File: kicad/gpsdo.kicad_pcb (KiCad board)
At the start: 2 copper layers, 76.2 x 30.5 mm, 54 parts, among them J1 Conn_Coaxial, J2 Conn_01x04_Male, J3 Conn_01x04_Male, J4 Conn_01x04_Male, J5 Conn_01x04_Male, J6 Conn_01x04_Male, U1 MSP430F5171IDA, U10 74AUC1G79, U11 47L64, U12 47L64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

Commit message: update pcb layout
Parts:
- removed C8: 100n, Resistor_SMD:R_0603_1608Metric
- removed R4, R5, R6, R7: 1.5k, Resistor_SMD:R_0603_1608Metric
- removed U5: LTC4317, Package_DFN_QFN:DFN-16-1EP_3x5mm_P0.5mm_EP1.66x4.4mm
- moved C21 0.78 mm to (77.5, 52.3), turned to 0 degrees
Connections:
- U1 pad 23: /EN2 -> Net-(U1-Pad23)
- U1 pad 24: /EN1 -> Net-(U1-Pad24)
- U11 pad 5: /SDA1 -> /SDA
- U11 pad 6: /SCL1 -> /SCL
- U11 pad 7: GND -> Net-(U11-Pad7)
- U12 pad 5: /SDA1 -> /SDA
- U12 pad 6: /SCL1 -> /SCL
- U2 pad 16: /SDA2 -> /SDA
- U2 pad 17: /SCL2 -> /SCL
- U3 pad 7: /SDA1 -> /SDA
- U3 pad 8: /SCL1 -> /SCL
- U4 pad 1: /SDA1 -> /SDA
- U4 pad 6: /SCL1 -> /SCL
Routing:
- net /SCL1: track 74.3 -> 0.00 mm, vias 4 -> 0
- net /SCL: track 15.3 -> 88.9 mm, vias 0 -> 4
- net /SDA1: track 73.0 -> 0.00 mm, vias 4 -> 0
- net /SDA: track 18.5 -> 90.2 mm, vias 2 -> 4
- net /SCL2: track 27.2 -> 0.00 mm, vias 4 -> 0
- net /EN2: track 25.5 -> 0.00 mm, vias 2 -> 0
- net /SDA2: track 25.4 -> 0.00 mm, vias 2 -> 0
- net /EN1: track 22.3 -> 0.00 mm, vias 2 -> 0
- net GND: track 70.1 -> 64.1 mm, vias 52 -> 48
- net +3V3: track 27.4 -> 25.3 mm, vias 2 -> 0
- net Net-(U11-Pad7): track 0.00 -> 1.64 mm, vias 0 -> 1
- net /uTXD: track 40.2 -> 39.4 mm
- net /uRXD: track 42.5 -> 41.9 mm
- net gPPS: track 21.3 -> 20.7 mm
- net Net-(C21-Pad2): track 2.59 -> 2.01 mm

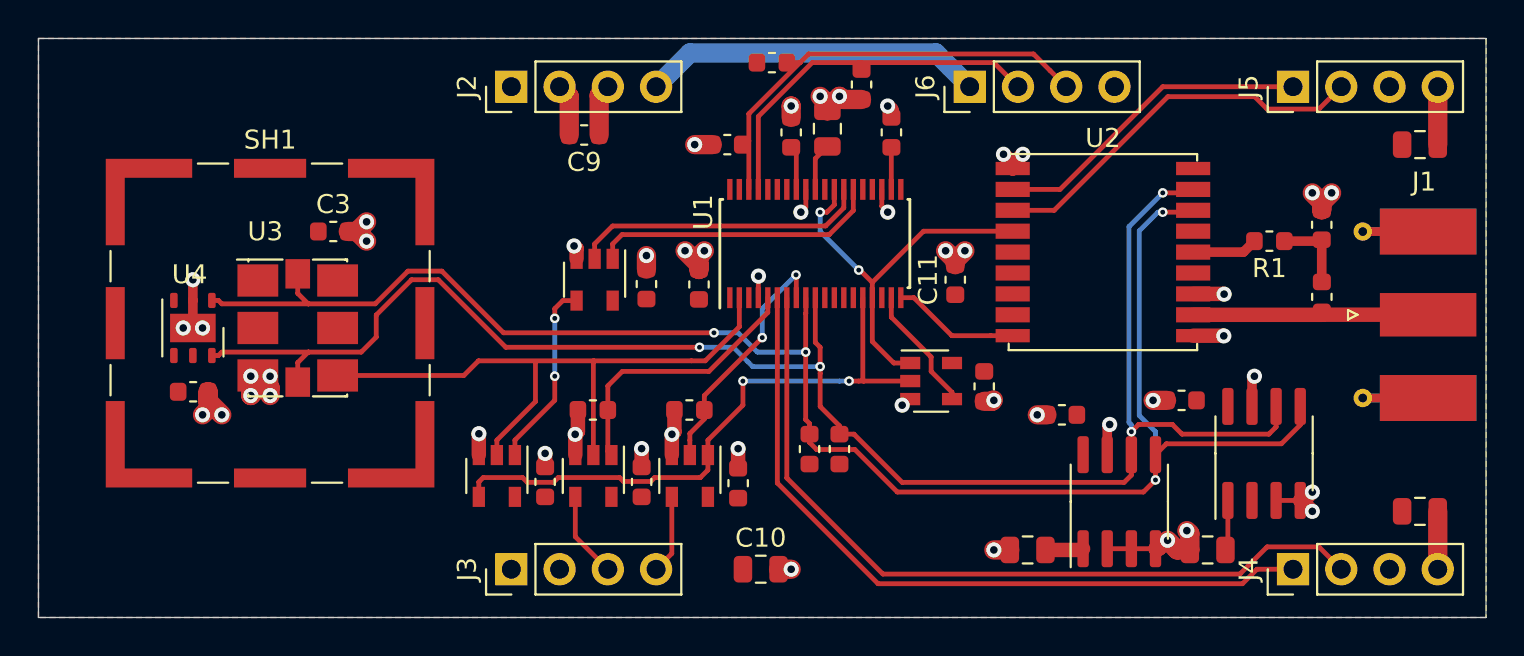
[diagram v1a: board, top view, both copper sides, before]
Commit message: remove extra EERAM
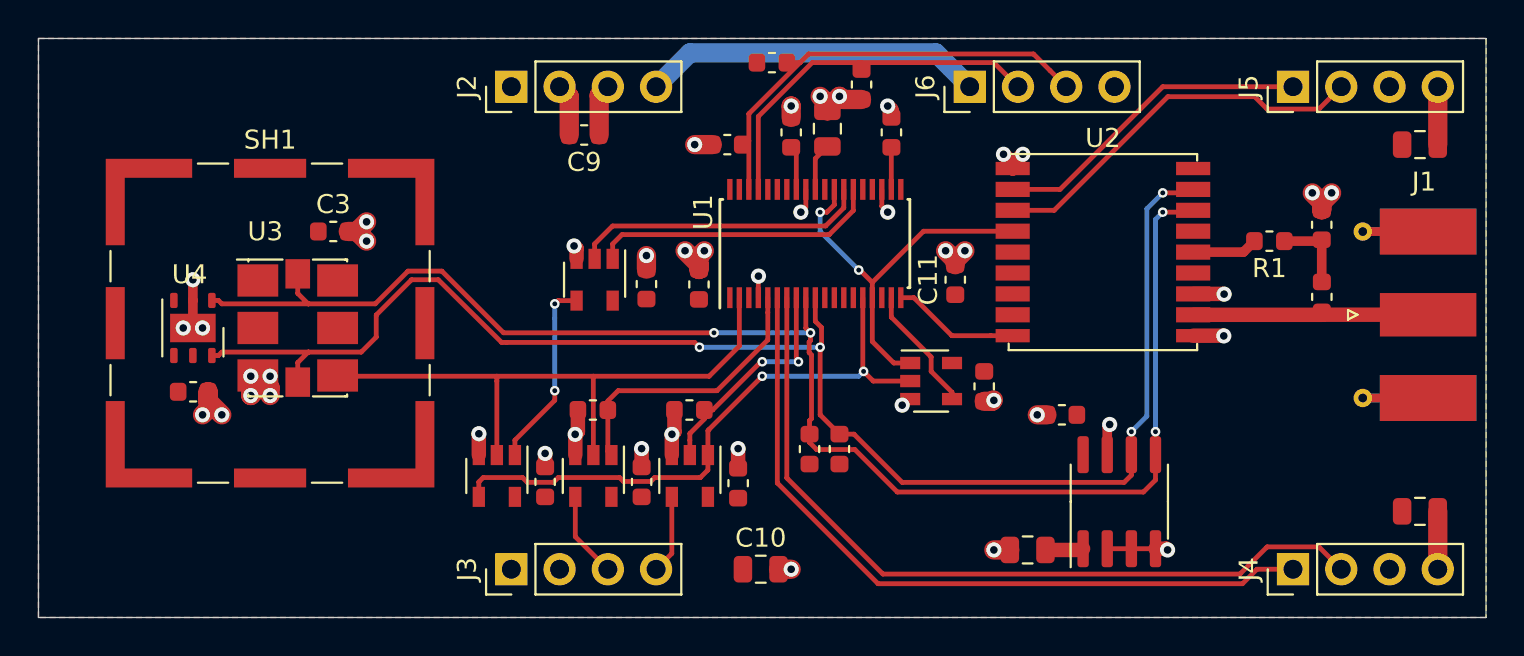
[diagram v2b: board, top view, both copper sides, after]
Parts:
- removed C16: 100n, Resistor_SMD:R_0603_1608Metric
- removed C22: 22u, Capacitor_SMD:C_0805_2012Metric
- removed U12: 47L64, Package_SO:SOIC-8_3.9x4.9mm_P1.27mm
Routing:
- net /SDA: track 90.2 -> 78.8 mm
- net /SCL: track 88.9 -> 79.2 mm
- net GND: track 64.1 -> 56.1 mm, vias 48 -> 43
- net Net-(C22-Pad2): track 2.66 -> 0.00 mm
- net CLK_25M: track 34.5 -> 32.7 mm
- net EN_PPS: track 13.0 -> 12.2 mm

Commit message: update pcb layout
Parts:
- C10, C19, C20: value 10u -> 22u
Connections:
- net Net-(J1-Pad1) renamed /gANT
- net Net-(U1-Pad19) renamed /gRST
- net Net-(U8-Pad1) renamed /uPPS
- U1 pad 11: Net-(U1-Pad11) -> +3V3
- U1 pad 12: Net-(U1-Pad12) -> +3V3
- U1 pad 13: Net-(U1-Pad13) -> +3V3
- U1 pad 14: Net-(U1-Pad14) -> +3V3
- U1 pad 2: CLK_25M -> Net-(U1-Pad2)
- U1 pad 20: Net-(U1-Pad20) -> +3V3
- U1 pad 23: Net-(U1-Pad23) -> +3V3
- U1 pad 24: Net-(U1-Pad24) -> +3V3
- U1 pad 3: Net-(U1-Pad3) -> CLK_25M
- U1 pad 32: Net-(U1-Pad32) -> +3V3
- U1 pad 33: Net-(U1-Pad33) -> +3V3
- U1 pad 34: Net-(U1-Pad34) -> +3V3
- U1 pad 37: Net-(U1-Pad37) -> +3V3
- U1 pad 38: Net-(U1-Pad38) -> +3V3
- U11 pad 7: Net-(U11-Pad7) -> GND
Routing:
- net Net-(U11-Pad7): track 1.64 -> 0.00 mm, vias 1 -> 0
- net GND: track 56.1 -> 57.5 mm, vias 43 -> 44
- net gPPS: track 20.7 -> 20.6 mm, vias 2 -> 3

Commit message: update pcb layout
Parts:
- removed C12, C13, C14, C15, C17, C9: 100n, Resistor_SMD:R_0603_1608Metric
- removed R8, R9: 15k, Resistor_SMD:R_0603_1608Metric
- removed U10, U8: 74AUC1G79, Package_TO_SOT_SMD:SOT-23-5
- removed U6, U7: 74LVC1G08, Package_TO_SOT_SMD:SOT-23-5
- removed U9: 74LVC1G86, Package_TO_SOT_SMD:SOT-23-5
- moved C10 24.3 mm to (53.9, 31.0), turned to 180 degrees
- moved C21 13.1 mm to (66.3, 45.5), turned to 90 degrees
- moved R3 12.5 mm to (78.2, 49.3)
- moved U11 11.4 mm to (71.4, 46.5), turned to 0 degrees
- moved R2 10.7 mm to (78.2, 46.3), turned to 270 degrees
- moved C18 3.07 mm to (76.2, 45.2), turned to 270 degrees
- moved C6 1.11 mm to (59.4, 39.1), turned to 180 degrees
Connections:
- J3 pad 3: /CLK -> CLK
- J3 pad 4: /PPS -> PPS
- U1 pad 15: oPPS -> PPS
- U1 pad 17: Net-(U1-Pad17) -> +3V3
- U1 pad 18: dPPS -> +3V3
- U1 pad 25: iPPS -> +3V3
- U1 pad 26: mPPS -> gPPS
- U1 pad 27: gPPS -> PPS
- U1 pad 3: CLK_25M -> CLK
- U1 pad 5: EN_CLK -> +3V3
- U1 pad 8: EN_PPS -> +3V3
- U3 pad 4: CLK_25M -> CLK
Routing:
- net CLK: track 0.00 -> 34.8 mm
- net CLK_25M: track 32.9 -> 0.00 mm
- net oPPS: track 31.6 -> 0.00 mm, vias 2 -> 0
- net PPS: track 0.00 -> 27.2 mm, vias 0 -> 2
- net mPPS: track 15.7 -> 0.00 mm
- net iPPS: track 15.3 -> 0.00 mm
- net EN_CLK: track 15.1 -> 0.00 mm
- net EN_PPS: track 12.2 -> 0.00 mm, vias 2 -> 0
- net GND: track 57.5 -> 46.8 mm, vias 44 -> 32
- net /uPPS: track 10.0 -> 0.00 mm, vias 2 -> 0
- net dPPS: track 6.66 -> 0.00 mm
- net gPPS: track 20.6 -> 14.5 mm, vias 3 -> 0
- net /SDA: track 79.0 -> 73.8 mm, vias 4 -> 2
- net /SCL: track 79.3 -> 74.7 mm, vias 4 -> 2
- net /CLK: track 4.52 -> 0.00 mm
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
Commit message: update pcb layout
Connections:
- U1 pad 15: PPS -> gPPS
- U1 pad 16: gPPS -> PPS
- U1 pad 17: +3V3 -> /gRST
- U1 pad 18: +3V3 -> PPS
- U1 pad 19: /gRST -> gPPS
- U1 pad 26: gPPS -> +3V3
- U1 pad 27: PPS -> +3V3
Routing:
- net PPS: track 27.2 -> 23.8 mm
- net gPPS: track 14.5 -> 11.5 mm
- net /gRST: track 7.19 -> 8.19 mm

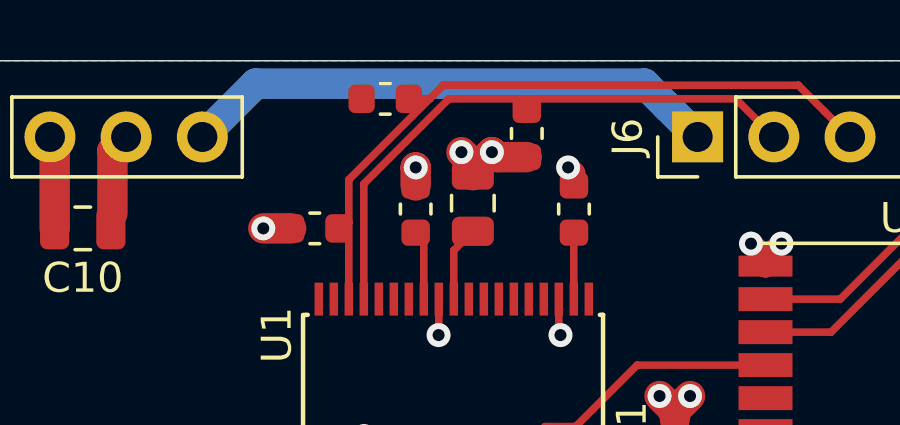
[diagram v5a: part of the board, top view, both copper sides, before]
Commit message: cleanup board layout
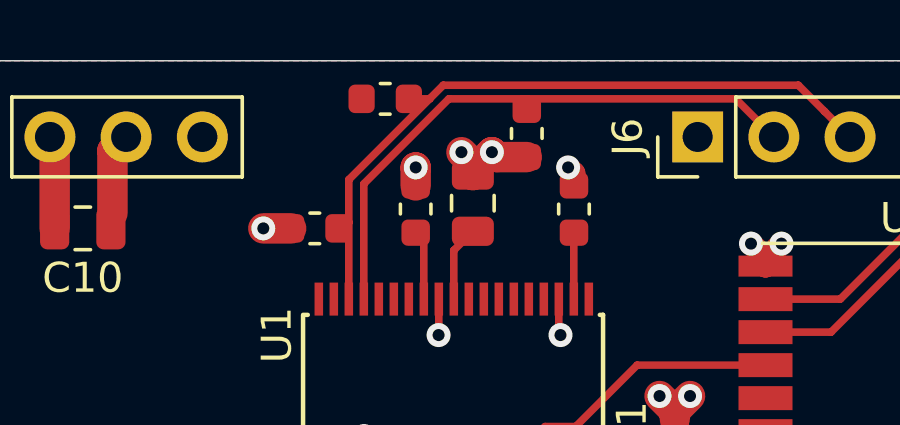
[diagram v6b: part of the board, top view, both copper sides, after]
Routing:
- net +3V3: track 27.1 -> 9.13 mm
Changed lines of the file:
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@@
     (thickness 1.6)
     (drawings 4)
-    (tracks 265)
+    (tracks 261)
     (zones 0)
     (modules 32)
@@
   (segment (start 54.915 28.397) (end 55.372 27.94) (width 1.016) (layer F.Cu) (net 2))
   (segment (start 54.915 30.48) (end 54.915 28.397) (width 1.016) (layer F.Cu) (net 2))
-  (segment (start 73.406 26.924) (end 74.422 27.94) (width 1.016) (layer B.Cu) (net 2))
-  (segment (start 72.644 26.162) (end 73.406 26.924) (width 1.016) (layer B.Cu) (net 2))
-  (segment (start 59.69 26.162) (end 72.644 26.162) (width 1.016) (layer B.Cu) (net 2))
-  (segment (start 57.912 27.94) (end 59.69 26.162) (width 1.016) (layer B.Cu) (net 2))
   (segment (start 65.294 39.045) (end 65.294 39.1) (width 0.254) (layer F.Cu) (net 2))
   (segment (start 63.794 39.045) (end 63.794 39.838) (width 0.254) (layer F.Cu) (net 2))

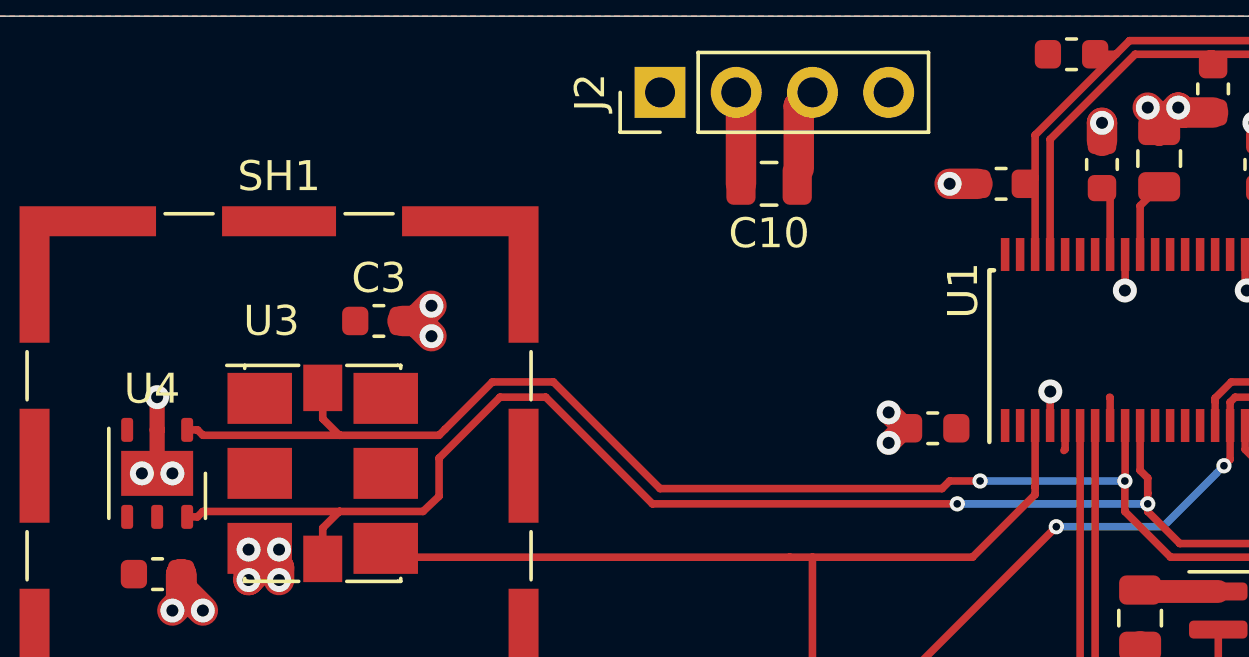
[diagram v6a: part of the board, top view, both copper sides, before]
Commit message: change Si549 to Si544
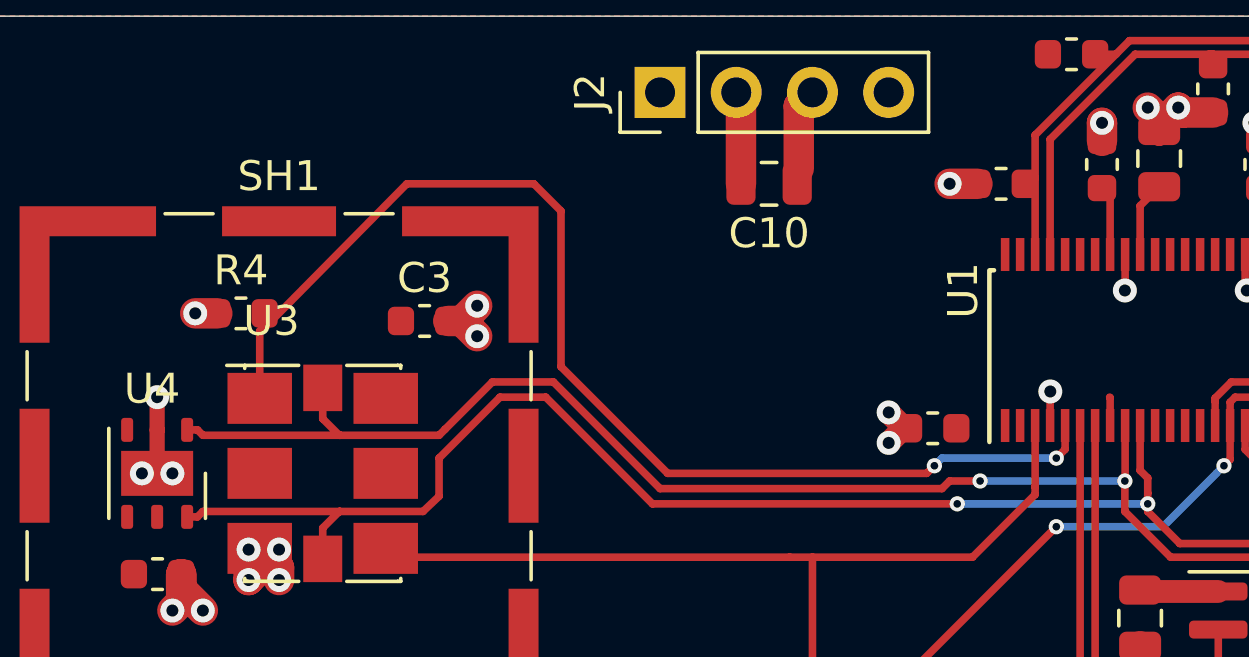
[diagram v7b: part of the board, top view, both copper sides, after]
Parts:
- added R4: 15k, Resistor_SMD:R_0603_1608Metric, F.Cu at (36.3, 35.3)
- moved C3 1.52 mm to (42.4, 35.6)
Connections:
- U1 pad 5: +3V3 -> OE_CLK
- U3 pad 1: +3V3 -> OE_CLK
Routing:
- net OE_CLK: track 0.00 -> 39.8 mm, vias 0 -> 2
- net +3V3: track 9.13 -> 8.28 mm
- net GND: track 46.8 -> 47.5 mm, vias 32 -> 33
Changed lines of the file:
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@@
     (thickness 1.6)
     (drawings 4)
-    (tracks 261)
+    (tracks 279)
     (zones 0)
-    (modules 32)
-    (nets 29)
+    (modules 33)
+    (nets 30)
   )
   (page A)
@@
   )
   (setup
-    (last_trace_width 0.25)
+    (last_trace_width 0.254)
     (user_trace_width 0.127)
     (user_trace_width 0.254)
@@
   (net 27 CLK)
   (net 28 PPS)
+  (net 29 OE_CLK)
   (net_class Default "This is the default net class."
     (clearance 0.2)
@@
     (add_net "Net-(U3-Pad5)")
     (add_net "Net-(U4-Pad3)")
+    (add_net OE_CLK)
     (add_net PPS)
     (add_net gPPS)
+  )
+  (module Resistor_SMD:R_0603_1608Metric (layer F.Cu)
+    (at 36.322 35.306)
+    (descr "Resistor SMD 0603 (1608 Metric), square (rectangular) end terminal, IPC_7351 nominal, (Body size source: http://www.tortai-tech.com/upload/download/2011102023233369053.pdf), generated with kicad-footprint-generator")
+    (tags resistor)
+    (attr smd)
+    (fp_text reference R4 (at 0 -1.43) (layer F.SilkS)
+      (effects (font (size 1 1) (thickness 0.15)))
+    )
+    (fp_text value 15k (at 0 1.43) (layer F.Fab) hide
+      (effects (font (size 1 1) (thickness 0.15)))
+    )
+    (fp_text user %R (at 0 0) (layer F.Fab)
+      (effects (font (size 0.4 0.4) (thickness 0.06)))
+    )
+    (fp_line (start 1.48 0.73) (end -1.48 0.73) (layer F.CrtYd) (width 0.05))
+    (fp_line (start 1.48 -0.73) (end 1.48 0.73) (layer F.CrtYd) (width 0.05))
+    (fp_line (start -1.48 -0.73) (end 1.48 -0.73) (layer F.CrtYd) (width 0.05))
+    (fp_line (start -1.48 0.73) (end -1.48 -0.73) (layer F.CrtYd) (width 0.05))
+    (fp_line (start -0.162779 0.51) (end 0.162779 0.51) (layer F.SilkS) (width 0.12))
+    (fp_line (start -0.162779 -0.51) (end 0.162779 -0.51) (layer F.SilkS) (width 0.12))
+    (fp_line (start 0.8 0.4) (end -0.8 0.4) (layer F.Fab) (width 0.1))
+    (fp_line (start 0.8 -0.4) (end 0.8 0.4) (layer F.Fab) (width 0.1))
+    (fp_line (start -0.8 -0.4) (end 0.8 -0.4) (layer F.Fab) (width 0.1))
+    (fp_line (start -0.8 0.4) (end -0.8 -0.4) (layer F.Fab) (width 0.1))
+    (pad 2 smd roundrect (at 0.7875 0) (size 0.875 0.95) (layers F.Cu F.Paste F.Mask) (roundrect_rratio 0.25)
+      (net 29 OE_CLK))
+    (pad 1 smd roundrect (at -0.7875 0) (size 0.875 0.95) (layers F.Cu F.Paste F.Mask) (roundrect_rratio 0.25)
+      (net 1 GND))
+    (model ${KISYS3DMOD}/Resistor_SMD.3dshapes/R_0603_1608Metric.wrl
+      (at (xyz 0 0 0))
+      (scale (xyz 1 1 1))
+      (rotate (xyz 0 0 0))
+    )
   )
   (module Package_SO:TSSOP-38_4.4x9.7mm_P0.5mm (layer F.Cu)
@@
       (net 20 /uTXD))
     (pad 5 smd rect (at -2.85 -2.5 90) (size 1.1 0.285) (layers F.Cu F.Paste F.Mask)
-      (net 2 +3V3))
+      (net 29 OE_CLK))
     (pad 4 smd rect (at -2.85 -3 90) (size 1.1 0.285) (layers F.Cu F.Paste F.Mask)
       (net 1 GND))
@@
   )
   (module Resistor_SMD:R_0603_1608Metric (layer F.Cu)
-    (at 40.9195 35.56)
+    (at 42.4435 35.56)
     (descr "Resistor SMD 0603 (1608 Metric), square (rectangular) end terminal, IPC_7351 nominal, (Body size source: http://www.tortai-tech.com/upload/download/2011102023233369053.pdf), generated with kicad-footprint-generator")
     (tags resistor)
@@
       (net 7 "Net-(U3-Pad2)"))
     (pad 1 smd rect (at -2.5 2.1 270) (size 1.7 2.15) (layers F.Cu F.Paste F.Mask)
-      (net 2 +3V3))
+      (net 29 OE_CLK))
     (model ${KISYS3DMOD}/Oscillator.3dshapes/Oscillator_SMD_SI570_SI571_Standard.wrl
       (at (xyz 0 0 0))
@@
   (segment (start 37.592 43.784) (end 36.948 43.14) (width 1.016) (layer F.Cu) (net 1))
   (segment (start 37.592 44.196) (end 37.592 43.784) (width 1.016) (layer F.Cu) (net 1))
-  (via (at 42.672 35.052) (size 0.8) (drill 0.4) (layers F.Cu B.Cu) (net 1))
-  (via (at 42.672 36.068) (size 0.8) (drill 0.4) (layers F.Cu B.Cu) (net 1))
-  (segment (start 42.164 35.56) (end 42.672 35.052) (width 1.016) (layer F.Cu) (net 1))
-  (segment (start 42.164 35.56) (end 42.672 36.068) (width 1.016) (layer F.Cu) (net 1))
-  (segment (start 41.707 35.56) (end 42.164 35.56) (width 1.016) (layer F.Cu) (net 1))
+  (via (at 44.196 35.052) (size 0.8) (drill 0.4) (layers F.Cu B.Cu) (net 1))
+  (via (at 44.196 36.068) (size 0.8) (drill 0.4) (layers F.Cu B.Cu) (net 1))
+  (segment (start 43.688 35.56) (end 44.196 35.052) (width 1.016) (layer F.Cu) (net 1))
+  (segment (start 43.688 35.56) (end 44.196 36.068) (width 1.016) (layer F.Cu) (net 1))
+  (segment (start 43.231 35.56) (end 43.688 35.56) (width 1.016) (layer F.Cu) (net 1))
   (via (at 57.912 38.608) (size 0.8) (drill 0.4) (layers F.Cu B.Cu) (net 1))
   (via (at 57.912 39.624) (size 0.8) (drill 0.4) (layers F.Cu B.Cu) (net 1))
@@
   (segment (start 54.915 30.48) (end 54.915 28.397) (width 1.016) (layer F.Cu) (net 2))
   (segment (start 65.294 39.045) (end 65.294 39.1) (width 0.254) (layer F.Cu) (net 2))
-  (segment (start 63.794 39.045) (end 63.794 39.838) (width 0.254) (layer F.Cu) (net 2))
-  (segment (start 63.794 39.838) (end 63.754 39.878) (width 0.254) (layer F.Cu) (net 2))
   (segment (start 65.294 39.045) (end 65.294 38.116) (width 0.254) (layer F.Cu) (net 2))
   (segment (start 65.294 38.116) (end 65.278 38.1) (width 0.254) (layer F.Cu) (net 2))
+  (via (at 34.798 35.306) (size 0.8) (drill 0.4) (layers F.Cu B.Cu) (net 1))
+  (segment (start 35.5345 35.306) (end 34.798 35.306) (width 1.016) (layer F.Cu) (net 1))
+  (via (at 59.436 40.386) (size 0.508) (drill 0.254) (layers F.Cu B.Cu) (net 29))
+  (via (at 63.5 40.132) (size 0.508) (drill 0.254) (layers F.Cu B.Cu) (net 29))
   (segment (start 88.829938 36.646062) (end 89.408 36.068) (width 0.508) (layer F.Cu) (net 4))
   (segment (start 86.183678 36.646062) (end 88.829938 36.646062) (width 0.508) (layer F.Cu) (net 4))
@@
   (segment (start 69.294 38.267498) (end 69.461498 38.1) (width 0.25) (layer F.Cu) (net 28))
   (segment (start 69.294 39.045) (end 69.294 38.267498) (width 0.25) (layer F.Cu) (net 28))
+  (segment (start 63.794 39.838) (end 63.5 40.132) (width 0.254) (layer F.Cu) (net 29))
+  (segment (start 63.794 39.045) (end 63.794 39.838) (width 0.254) (layer F.Cu) (net 29))
+  (segment (start 59.69 40.132) (end 63.5 40.132) (width 0.254) (layer B.Cu) (net 29))
+  (segment (start 59.436 40.386) (end 59.69 40.132) (width 0.254) (layer B.Cu) (net 29))
+  (segment (start 46.082602 30.988) (end 41.851398 30.988) (width 0.254) (layer F.Cu) (net 29))
+  (segment (start 46.99 31.895398) (end 46.082602 30.988) (width 0.254) (layer F.Cu) (net 29))
+  (segment (start 36.948 35.891398) (end 36.948 37.036) (width 0.254) (layer F.Cu) (net 29))
+  (segment (start 50.546 40.64) (end 46.99 37.084) (width 0.254) (layer F.Cu) (net 29))
+  (segment (start 36.948 37.036) (end 36.948 38.14) (width 0.254) (layer F.Cu) (net 29))
+  (segment (start 46.99 37.084) (end 46.99 31.895398) (width 0.254) (layer F.Cu) (net 29))
+  (segment (start 59.182 40.64) (end 50.546 40.64) (width 0.254) (layer F.Cu) (net 29))
+  (segment (start 59.436 40.386) (end 59.182 40.64) (width 0.254) (layer F.Cu) (net 29))
+  (segment (start 37.1095 35.7885) (end 37.084 35.814) (width 0.254) (layer F.Cu) (net 29))
+  (segment (start 37.1095 35.306) (end 37.1095 35.7885) (width 0.254) (layer F.Cu) (net 29))
+  (segment (start 37.084 35.814) (end 36.948 35.891398) (width 0.254) (layer F.Cu) (net 29))
+  (segment (start 41.851398 30.988) (end 37.084 35.814) (width 0.254) (layer F.Cu) (net 29))
   (zone (net 2) (net_name +3V3) (layer F.Cu) (hatch edge 0.508)
     (connect_pads yes (clearance 0.254))
